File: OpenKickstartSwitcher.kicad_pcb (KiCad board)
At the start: 2 copper layers, 28.1 x 69.1 mm, 10 parts, among them J1 Conn_01x03, J2 Conn_01x03, J99 OSHW_LOGO, U1 KS_SOCKET, U2 M27C800, U3 7400

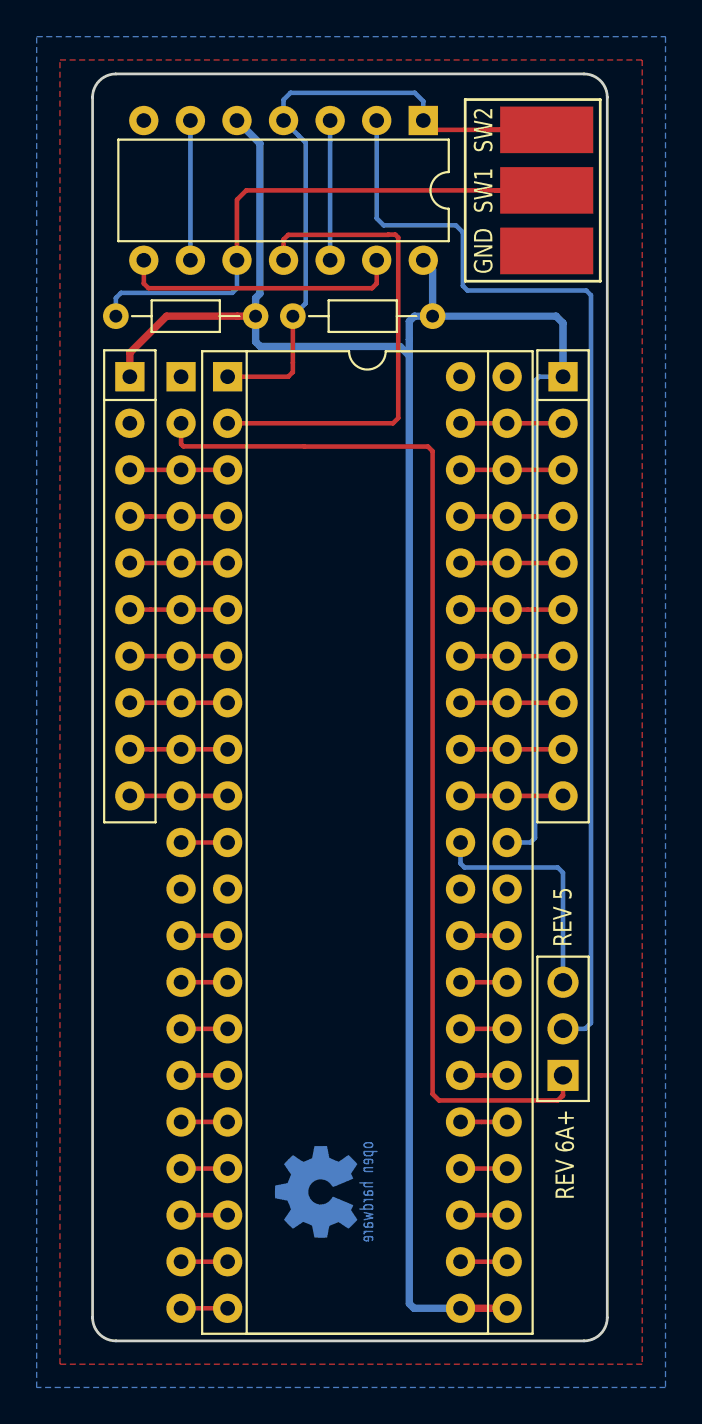
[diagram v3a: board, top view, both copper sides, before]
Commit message: Slight corner fixes
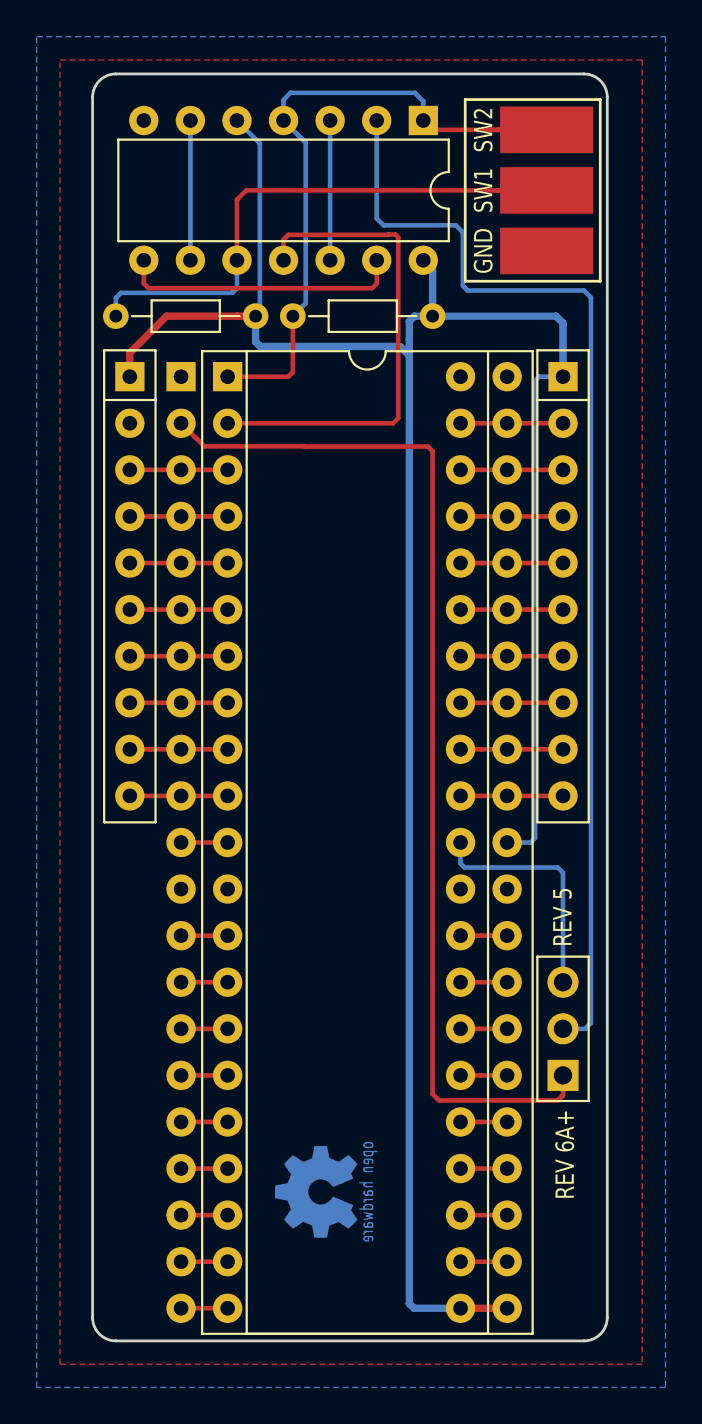
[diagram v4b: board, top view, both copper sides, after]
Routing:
- net Net-(J1-Pad1): track 58.5 -> 57.9 mm
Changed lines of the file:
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@@
     (arrow2b (pts (xy 164.084 163.068) (xy 165.210504 162.481579)))
   )
-  (segment (start 148.844 107.442) (end 148.844 108.57337) (width 0.25) (layer F.Cu) (net 1))
+  (segment (start 150.114 108.70037) (end 155.56337 108.70037) (width 0.25) (layer F.Cu) (net 1))
+  (segment (start 148.844 107.442) (end 149.643999 108.241999) (width 0.25) (layer F.Cu) (net 1))
+  (segment (start 149.643999 108.241999) (end 149.655629 108.241999) (width 0.25) (layer F.Cu) (net 1))
+  (segment (start 149.655629 108.241999) (end 150.114 108.70037) (width 0.25) (layer F.Cu) (net 1))
+  (segment (start 169.672 144.102) (end 169.672 143.002) (width 0.25) (layer F.Cu) (net 1))
   (segment (start 155.575 108.712) (end 162.306 108.712) (width 0.25) (layer F.Cu) (net 1))
-  (segment (start 148.844 108.57337) (end 148.971 108.70037) (width 0.25) (layer F.Cu) (net 1))
-  (segment (start 148.971 108.70037) (end 155.56337 108.70037) (width 0.25) (layer F.Cu) (net 1))
+  (segment (start 162.56 108.966) (end 162.56 144.018) (width 0.25) (layer F.Cu) (net 1))
+  (segment (start 162.908999 144.366999) (end 169.385999 144.366999) (width 0.25) (layer F.Cu) (net 1))
   (segment (start 155.56337 108.70037) (end 155.575 108.712) (width 0.25) (layer F.Cu) (net 1))
   (segment (start 162.306 108.712) (end 162.56 108.966) (width 0.25) (layer F.Cu) (net 1))
-  (segment (start 162.56 108.966) (end 162.56 144.018) (width 0.25) (layer F.Cu) (net 1))
-  (segment (start 169.672 144.102) (end 169.672 143.002) (width 0.25) (layer F.Cu) (net 1))
   (segment (start 162.56 144.018) (end 162.908999 144.366999) (width 0.25) (layer F.Cu) (net 1))
-  (segment (start 169.629 144.145) (end 169.672 144.102) (width 0.25) (layer F.Cu) (net 1))
-  (segment (start 162.908999 144.366999) (end 169.385999 144.366999) (width 0.25) (layer F.Cu) (net 1))
   (segment (start 169.385999 144.366999) (end 169.607998 144.145) (width 0.25) (layer F.Cu) (net 1))
   (segment (start 169.607998 144.145) (end 169.629 144.145) (width 0.25) (layer F.Cu) (net 1))
+  (segment (start 169.629 144.145) (end 169.672 144.102) (width 0.25) (layer F.Cu) (net 1))
   (segment (start 159.512 90.932) (end 159.512 96.266) (width 0.25) (layer B.Cu) (net 2))
+  (segment (start 159.512 96.266) (end 159.893 96.647) (width 0.25) (layer B.Cu) (net 2))
+  (segment (start 164.211 97.028) (end 164.211 99.949) (width 0.25) (layer B.Cu) (net 2))
+  (segment (start 159.893 96.647) (end 163.83 96.647) (width 0.25) (layer B.Cu) (net 2))
+  (segment (start 171.196 100.584) (end 171.196 140.140081) (width 0.25) (layer B.Cu) (net 2))
+  (segment (start 163.83 96.647) (end 164.211 97.028) (width 0.25) (layer B.Cu) (net 2))
+  (segment (start 164.211 99.949) (end 164.465 100.203) (width 0.25) (layer B.Cu) (net 2))
+  (segment (start 164.465 100.203) (end 170.815 100.203) (width 0.25) (layer B.Cu) (net 2))
   (segment (start 171.196 140.140081) (end 170.874081 140.462) (width 0.25) (layer B.Cu) (net 2))
-  (segment (start 159.512 96.266) (end 159.893 96.647) (width 0.25) (layer B.Cu) (net 2))
-  (segment (start 159.893 96.647) (end 163.83 96.647) (width 0.25) (layer B.Cu) (net 2))
-  (segment (start 163.83 96.647) (end 164.211 97.028) (width 0.25) (layer B.Cu) (net 2))
-  (segment (start 164.211 97.028) (end 164.211 99.949) (width 0.25) (layer B.Cu) (net 2))
-  (segment (start 164.211 99.949) (end 164.465 100.203) (width 0.25) (layer B.Cu) (net 2))
-  (segment (start 164.465 100.203) (end 170.942 100.203) (width 0.25) (layer B.Cu) (net 2))
-  (segment (start 170.942 100.203) (end 171.196 100.457) (width 0.25) (layer B.Cu) (net 2))
+  (segment (start 170.815 100.203) (end 171.196 100.584) (width 0.25) (layer B.Cu) (net 2))
   (segment (start 170.874081 140.462) (end 169.672 140.462) (width 0.25) (layer B.Cu) (net 2))
-  (segment (start 171.196 100.457) (end 171.196 140.140081) (width 0.25) (layer B.Cu) (net 2))
   (segment (start 164.084 130.302) (end 164.084 131.445) (width 0.25) (layer B.Cu) (net 3))
   (segment (start 169.672 131.953) (end 169.672 137.922) (width 0.25) (layer B.Cu) (net 3))
@@
   (segment (start 145.288 101.6) (end 145.288 100.610051) (width 0.25) (layer B.Cu) (net 5))
   (segment (start 145.288 100.610051) (end 145.568051 100.33) (width 0.25) (layer B.Cu) (net 5))
-  (segment (start 151.892 90.932) (end 153.142001 92.182001) (width 0.4) (layer B.Cu) (net 7))
-  (segment (start 153.142001 92.182001) (end 153.142001 100.37605) (width 0.4) (layer B.Cu) (net 7))
+  (segment (start 151.892 90.932) (end 153.142001 92.182001) (width 0.25) (layer B.Cu) (net 7))
+  (segment (start 153.142001 92.182001) (end 153.142001 101.365999) (width 0.25) (layer B.Cu) (net 7))
+  (segment (start 153.142001 101.365999) (end 152.908 101.6) (width 0.25) (layer B.Cu) (net 7))
   (segment (start 160.655 103.251) (end 160.782 103.251) (width 0.4) (layer B.Cu) (net 7))
   (segment (start 153.162 103.251) (end 160.655 103.251) (width 0.4) (layer B.Cu) (net 7))
@@
   (segment (start 161.29 155.448) (end 161.544 155.702) (width 0.4) (layer B.Cu) (net 7))
   (segment (start 161.544 155.702) (end 164.084 155.702) (width 0.4) (layer B.Cu) (net 7))
-  (segment (start 153.142001 100.37605) (end 152.908 100.610051) (width 0.4) (layer B.Cu) (net 7))
-  (segment (start 152.908 100.610051) (end 152.908 101.6) (width 0.4) (layer B.Cu) (net 7))
   (segment (start 152.908 101.6) (end 152.908 102.997) (width 0.4) (layer B.Cu) (net 7))
   (segment (start 152.908 102.997) (end 153.162 103.251) (width 0.4) (layer B.Cu) (net 7))

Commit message: Added capacitor, more space for resistors and minor adjustments
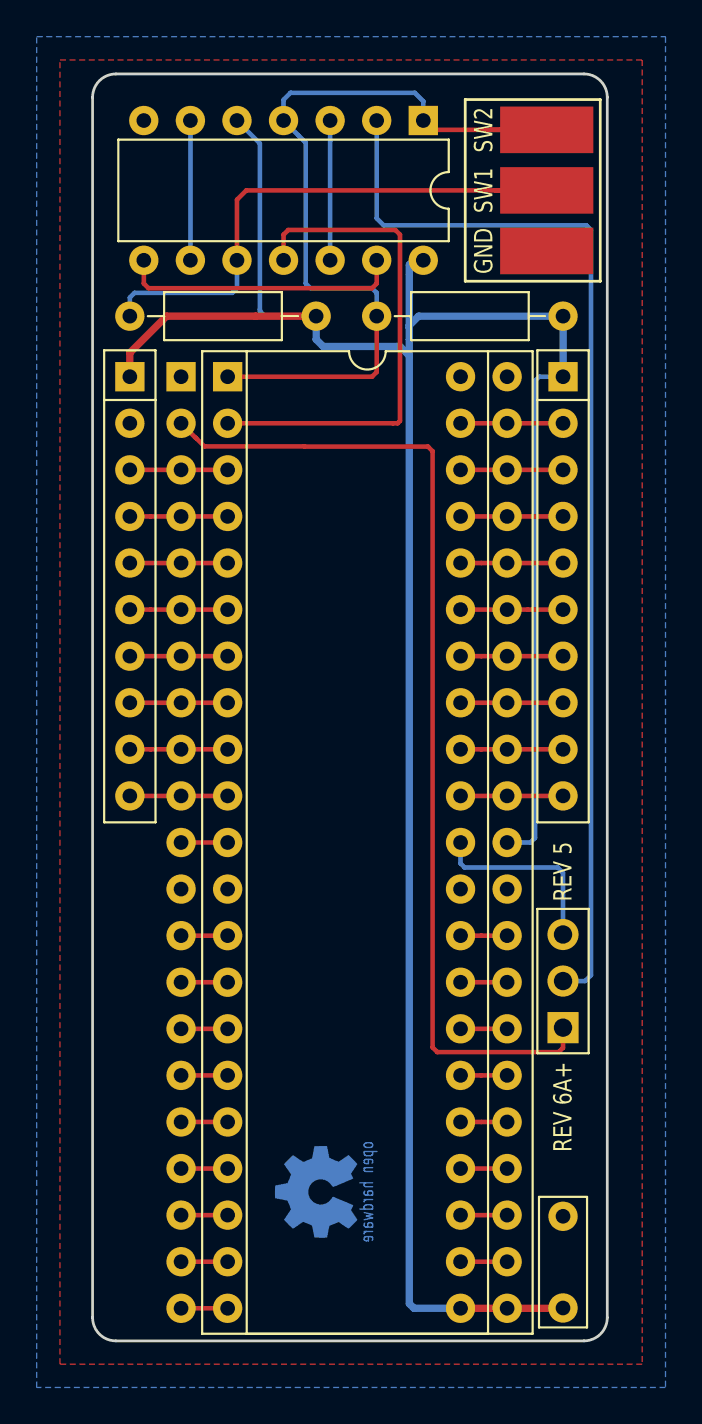
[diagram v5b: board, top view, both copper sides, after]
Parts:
- added C1: 100u, Capacitors_THT:C_Disc_D7.0mm_W2.5mm_P5.00mm, F.Cu at (169.7, 155.7)
- R1, R2: footprint Resistors_THT:R_Axial_DIN0204_L3.6mm_D1.6mm_P7.62mm_Horizontal -> Resistors_THT:R_Axial_DIN0207_L6.3mm_D2.5mm_P10.16mm_Horizontal
- moved R1 7.11 mm to (169.7, 101.6)
- moved R2 3.30 mm to (156.2, 101.6)
- moved J1 2.60 mm to (169.7, 140.4)
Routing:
- net /sw18: track 37.8 -> 45.7 mm
- net VCC: track 132.4 -> 139.3 mm
- net Net-(J1-Pad3): track 12.9 -> 10.3 mm
- net Net-(J1-Pad1): track 57.9 -> 55.3 mm
- net Net-(J1-Pad2): track 61.7 -> 59.6 mm
- net /sw17: track 32.0 -> 31.3 mm
- net Net-(U2-Pad2): track 26.8 -> 27.6 mm
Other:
- board text added: "V1"

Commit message: Add capacitor on 7400 I don't like this too much, tracks under the 7400 are pretty messy. Let's see if we can come up with something better.
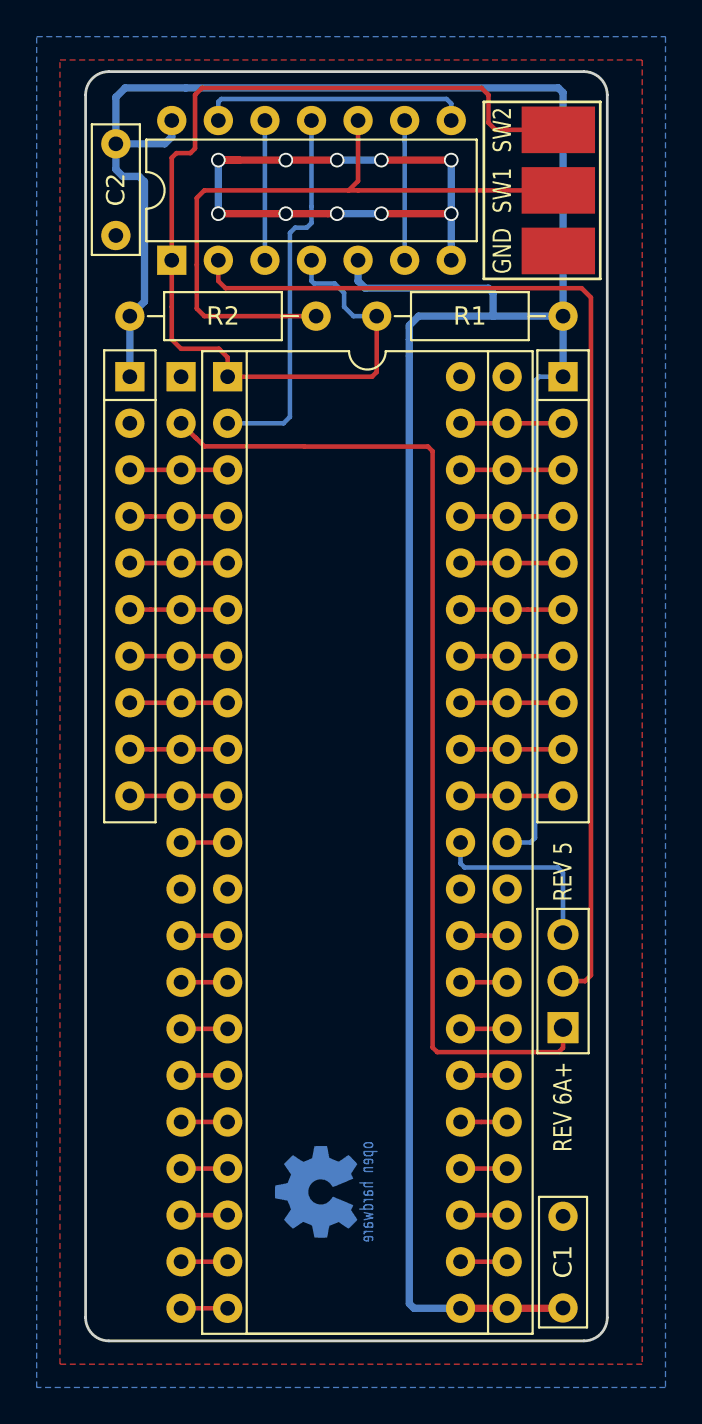
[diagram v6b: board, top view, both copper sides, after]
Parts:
- added C2: 100n, Capacitors_THT:C_Disc_D7.0mm_W2.5mm_P5.00mm, F.Cu at (145.3, 92.2)
- C1: value 100u -> 100n
- moved U3 15.7 mm to (148.3, 98.6), turned to 90 degrees
- moved R2 10.2 mm to (146.1, 101.6), turned to 0 degrees
- moved J2 0.64 mm to (169.4, 94.8)
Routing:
- net GND: track 0.00 -> 34.9 mm, vias 0 -> 10
- net VCC: track 139.3 -> 169.7 mm
- net /sw18: track 45.7 -> 57.8 mm
- net Net-(U2-Pad2): track 27.6 -> 20.6 mm
- net /sw17: track 31.3 -> 36.6 mm
- net Net-(J1-Pad2): track 59.6 -> 60.4 mm
- net Net-(U3-Pad13): track 15.5 -> 14.8 mm
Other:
- board size 28.1 x 69.1 mm -> 28.4 x 69.2 mm

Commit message: Much better now :)
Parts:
- removed J99: OSHW_LOGO, w_logo:Logo_copper_OSHW_6x6mm
- moved J2 0.25 mm to (169.2, 94.8)
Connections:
- J1 pad 2: Net-(J1-Pad2) -> /a17
- U3 pad 1: /sw18 -> Net-(U3-Pad1)
- U3 pad 10: /sw17 -> VCC
- U3 pad 11: Net-(U2-Pad2) -> Net-(U3-Pad11)
- U3 pad 13: Net-(U3-Pad13) -> /sw17
- U3 pad 2: Net-(J1-Pad2) -> Net-(U3-Pad11)
- U3 pad 3: Net-(U3-Pad12) -> Net-(U2-Pad2)
- U3 pad 4: /sw18 -> /a17
- U3 pad 5: VCC -> /sw18
- U3 pad 6: Net-(U3-Pad6) -> Net-(U3-Pad1)
- U3 pad 8: Net-(U3-Pad13) -> Net-(U3-Pad12)
- U3 pad 9: Net-(U3-Pad6) -> /sw18
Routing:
- net GND: track 34.9 -> 110.2 mm, vias 10 -> 40
- net Net-(J1-Pad2): track 60.4 -> 0.00 mm
- net /a17: track 0.00 -> 59.7 mm
- net /sw18: track 57.8 -> 35.6 mm
- net VCC: track 169.7 -> 153.2 mm
- net Net-(U3-Pad1): track 0.00 -> 14.9 mm
- net Net-(U3-Pad13): track 14.8 -> 0.00 mm
- net Net-(U3-Pad11): track 0.00 -> 12.4 mm
- net Net-(U2-Pad2): track 20.6 -> 12.3 mm
- net Net-(U3-Pad6): track 7.62 -> 0.00 mm
- net Net-(U3-Pad12): track 7.62 -> 14.2 mm
- net /sw17: track 36.6 -> 30.3 mm
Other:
- board size 28.4 x 69.2 mm -> 28.4 x 68.8 mm

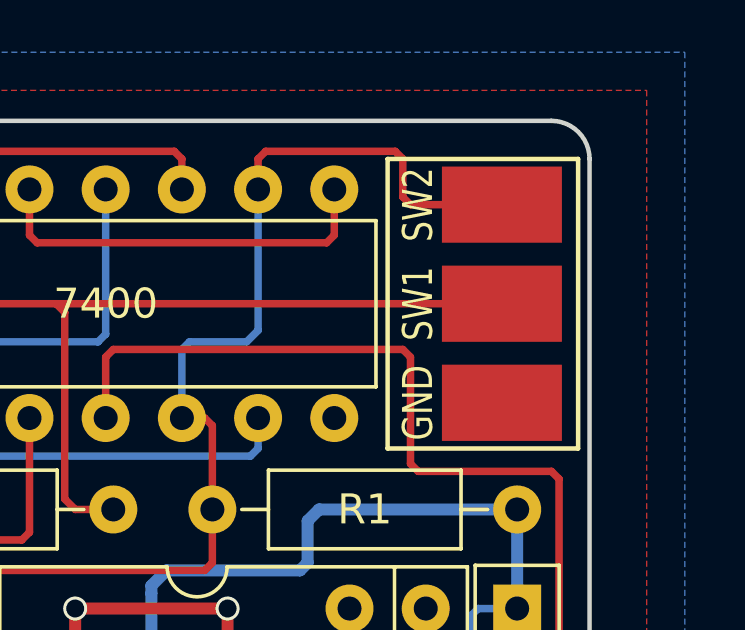
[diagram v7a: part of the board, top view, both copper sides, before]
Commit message: Re-add OSHW logo
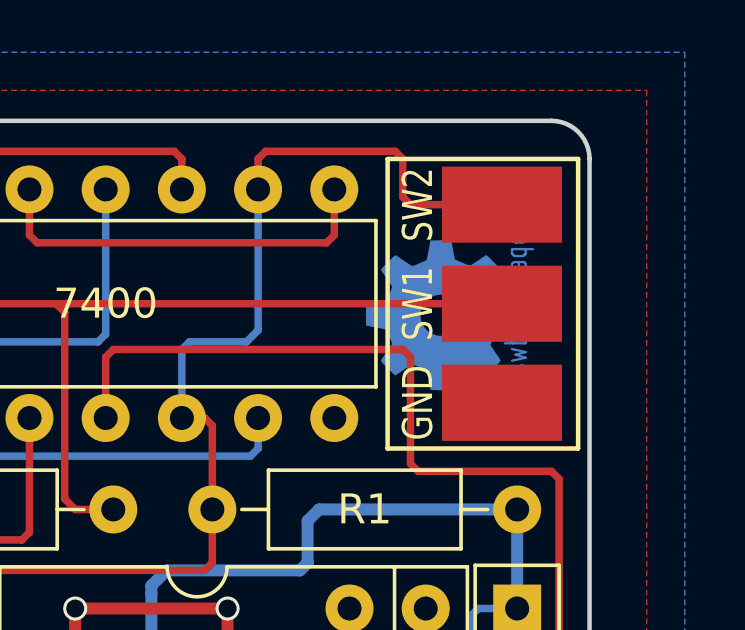
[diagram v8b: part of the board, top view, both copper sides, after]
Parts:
- added J99: OSHW_LOGO, w_logo:Logo_copper_OSHW_6x6mm, B.Cu at (166.9, 95.1)
